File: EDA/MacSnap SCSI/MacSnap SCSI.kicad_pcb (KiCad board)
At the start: 2 copper layers, 84 x 88 mm, 26 parts, among them IC1 Z53C8003VSG, J1 SCSI IDC-50, J2 SCSI IDC-26, U1 MB_LOW, U2 MB_HI, U3 ROM_LOW, U4 ROM_HI, U5 ATF16V8B, U6 ATF16V8B

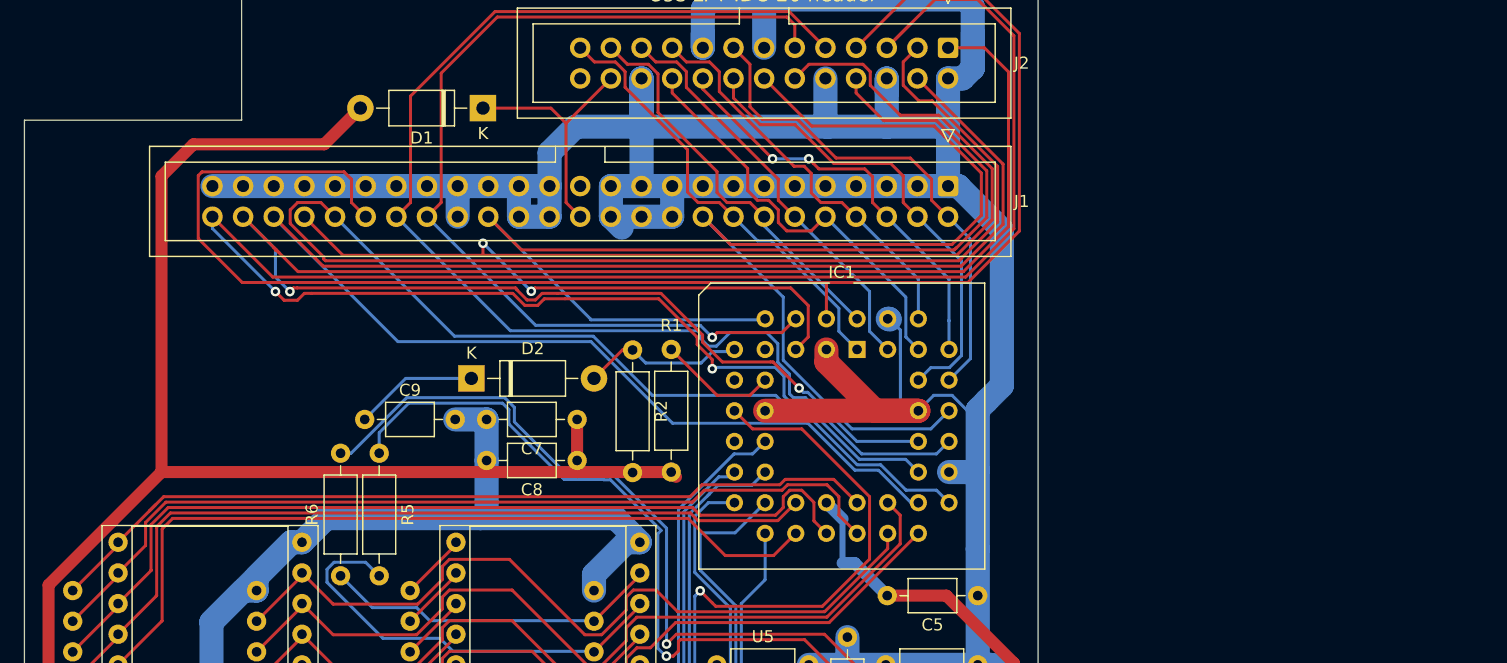
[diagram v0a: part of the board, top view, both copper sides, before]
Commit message: added resistor networks + TMPWR
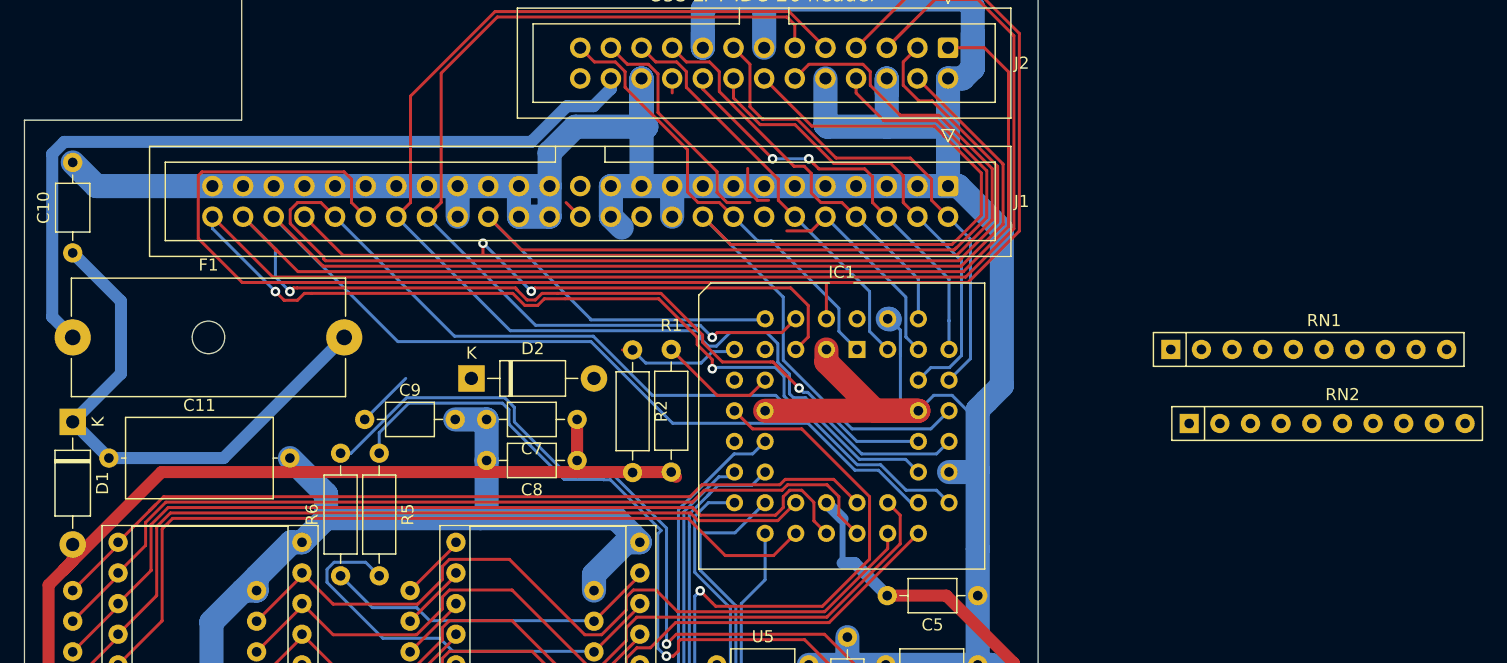
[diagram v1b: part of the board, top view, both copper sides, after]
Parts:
- added C10: 100nF, Capacitor_THT:C_Axial_L3.8mm_D2.6mm_P7.50mm_Horizontal, F.Cu at (64.0, 75.0)
- added C11: 2.2uF, Capacitor_THT:C_Axial_L12.0mm_D6.5mm_P15.00mm_Horizontal, F.Cu at (67.0, 92.0)
- added F1: Fuse 1.25A, Fuse:Fuseholder_Cylinder-5x20mm_Schurter_0031_8201_Horizontal_Open, F.Cu at (64.0, 82.0)
- added RN1: 4610X-101-111LF, Resistor_THT:R_Array_SIP10, F.Cu at (155.0, 83.0)
- added RN2: 4610X-101-111LF, Resistor_THT:R_Array_SIP10, F.Cu at (156.5, 89.1)
- D1: value 1N4001 -> D
- moved D1 42.8 mm to (64.0, 89.0), turned to 270 degrees
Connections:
- D1 pad 1: /TMPWR -> Net-(C10-Pad1)
- J1 pad 26: /TMPWR -> TMPWR
- J2 pad 24: /TMPWR -> TMPWR
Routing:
- net TMPWR: track 0.00 -> 67.0 mm
- net Net-(C10-Pad1): track 0.00 -> 45.2 mm
- net VCC: track 286.1 -> 245.1 mm
- net /TMPWR: track 20.9 -> 0.00 mm
- net /DB6: track 33.0 -> 19.7 mm
- net /DB4: track 35.0 -> 23.0 mm
- net Net-(C9-Pad1): track 10.2 -> 4.81 mm
- net Net-(D2-Pad2): track 13.5 -> 10.2 mm
- net GND: track 493.1 -> 491.6 mm

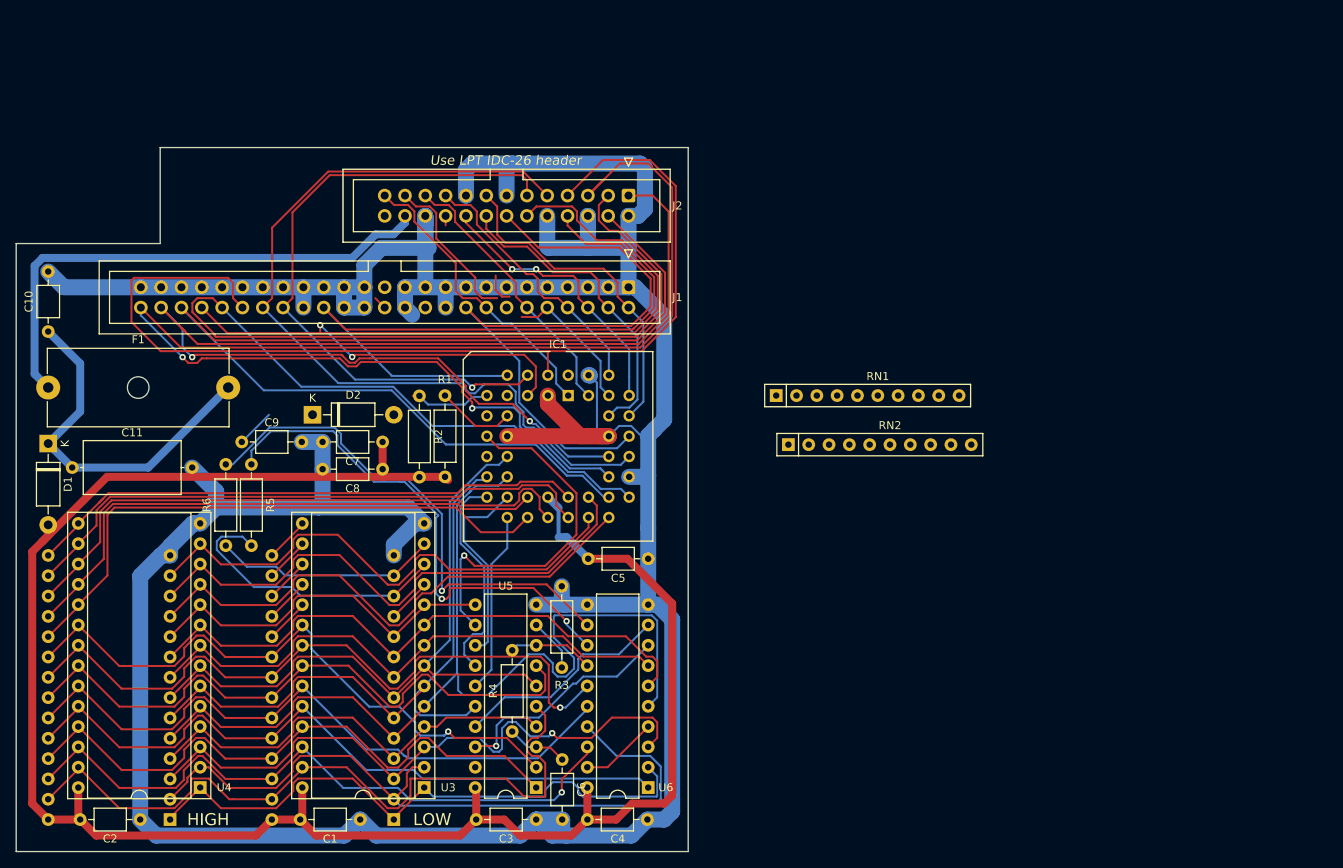
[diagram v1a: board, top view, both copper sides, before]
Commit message: added active SCSI termination to schema
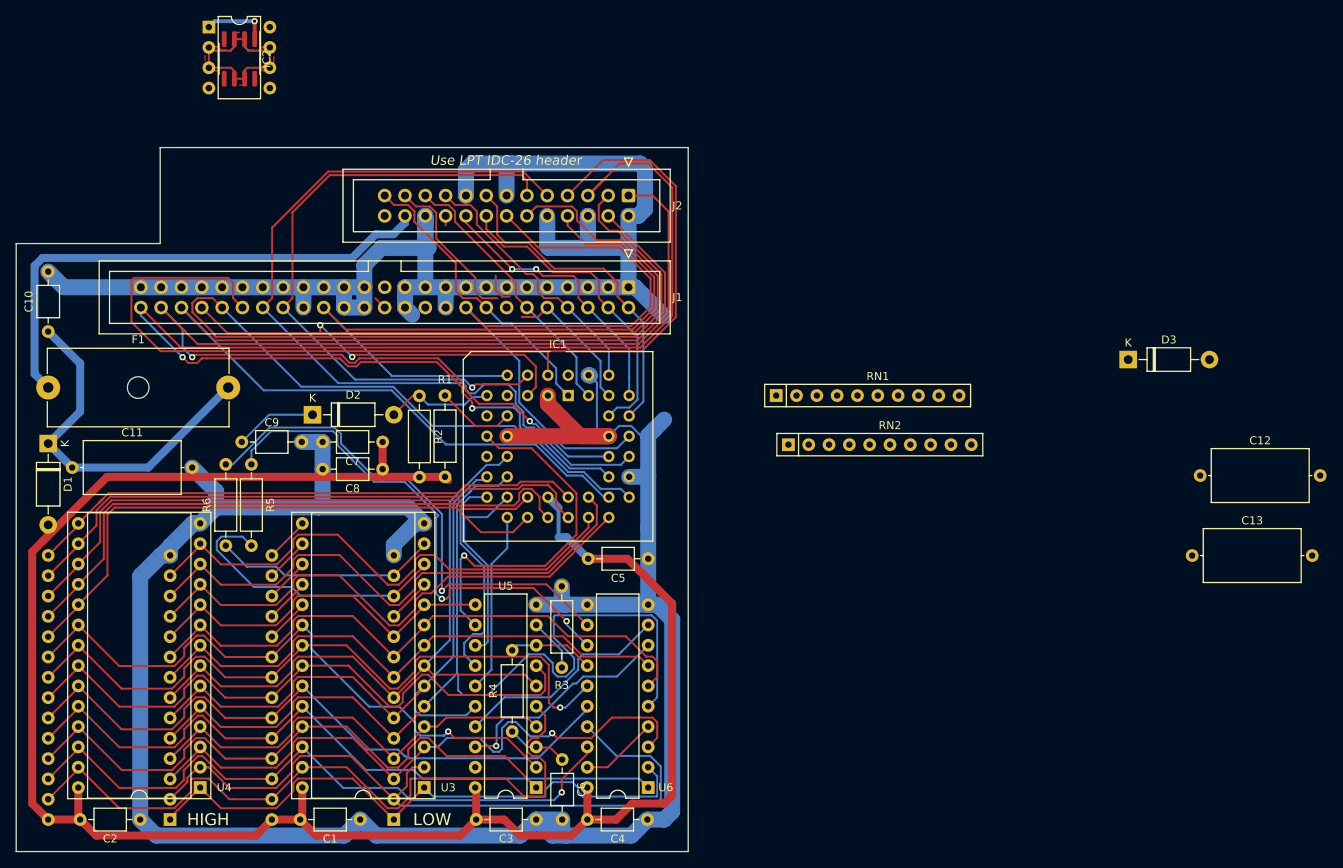
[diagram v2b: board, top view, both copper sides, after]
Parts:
- added C12: 10uF, Capacitor_THT:C_Axial_L12.0mm_D6.5mm_P15.00mm_Horizontal, F.Cu at (208.0, 93.0)
- added C13: 10uF, Capacitor_THT:C_Axial_L12.0mm_D6.5mm_P15.00mm_Horizontal, F.Cu at (207.0, 103.0)
- added D3: 1N5819, Diode_THT:D_DO-41_SOD81_P10.16mm_Horizontal, F.Cu at (199.0, 78.5)
- added IC2: MC34268DR2G, Package_SO:SOIC-8_3.9x4.9mm_P1.27mm, F.Cu at (87.9, 40.9)
- added IC3: MC34268DR2G, Package_DIP:DIP-8_W7.62mm, F.Cu at (84.1, 36.9)
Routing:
- net +2V8: track 0.00 -> 25.3 mm
- net Net-(C9-Pad1): track 4.81 -> 10.2 mm
- net GND: track 491.6 -> 487.0 mm, vias 0 -> 1
- net Net-(D2-Pad2): track 10.2 -> 13.5 mm
- added copper zone on F.Cu, net +2V8

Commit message: removed a few vias and router resistor packs. Moves Z53C80 further down
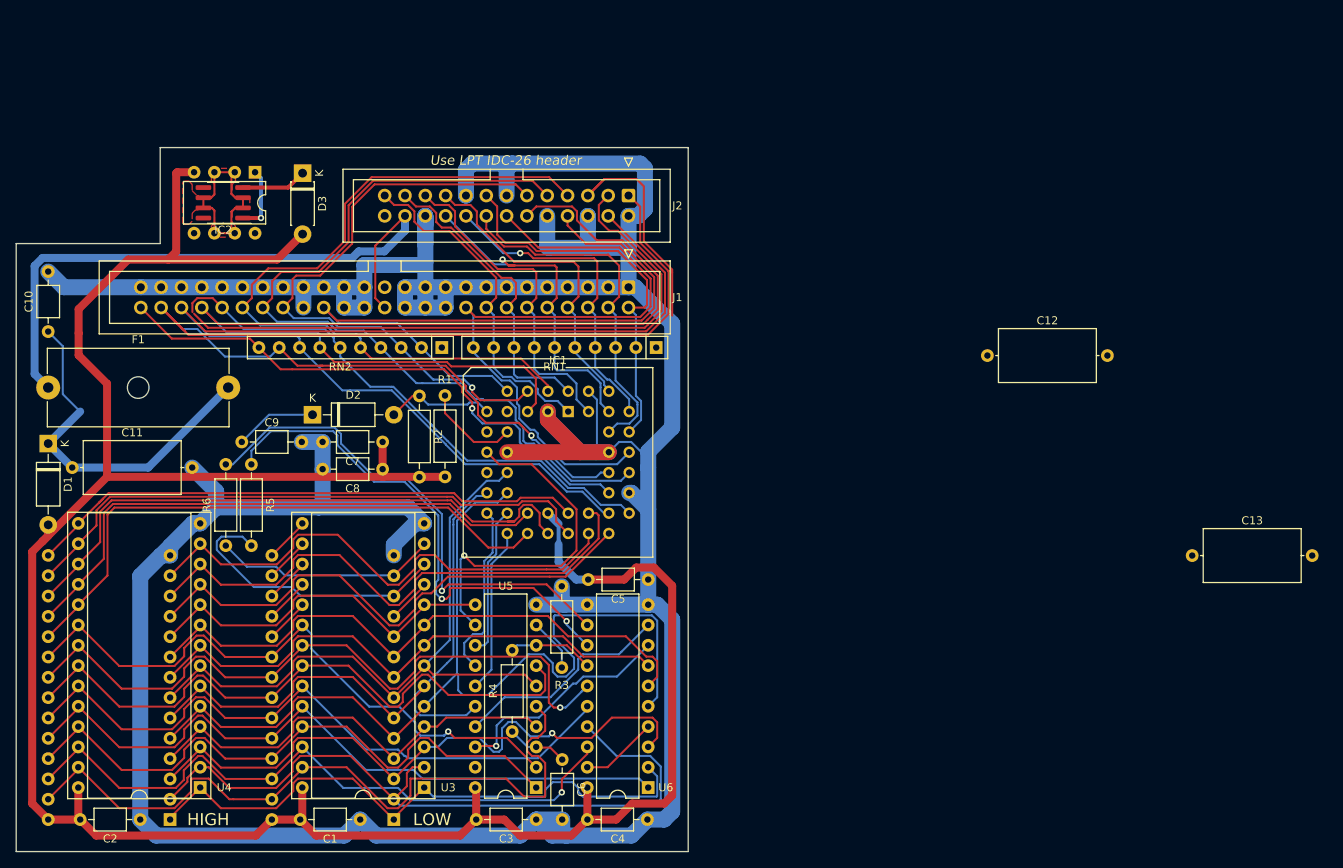
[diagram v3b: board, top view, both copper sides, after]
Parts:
- D3: footprint Diode_THT:D_DO-41_SOD81_P10.16mm_Horizontal -> Diode_THT:D_DO-41_SOD81_P7.62mm_Horizontal
- moved D3 105.8 mm to (95.8, 55.2), turned to 270 degrees
- moved RN2 45.0 mm to (113.2, 77.0), turned to 180 degrees
- moved C12 30.5 mm to (181.4, 78.0)
- moved IC3 19.0 mm to (89.9, 55.1), turned to 270 degrees
- moved IC2 18.1 mm to (85.9, 58.9), turned to 180 degrees
- moved RN1 16.2 mm to (140.0, 77.0), turned to 180 degrees
- moved C5 2.60 mm to (139.0, 106.0)
- moved IC1 2.00 mm to (129.0, 85.0)
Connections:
- RN2 pad 10: /~MSG -> /~IO
- RN2 pad 3: /~SEL -> /~BSY
- RN2 pad 4: /~BSY -> /~ACK
- RN2 pad 6: /~REQ -> /~MSG
- RN2 pad 7: /~ACK -> /~SEL
- RN2 pad 8: /~IO -> /~CD
- RN2 pad 9: /~CD -> /~REQ
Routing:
- net /~IO: track 173.0 -> 99.0 mm, vias 2 -> 1
- net VCC: track 245.1 -> 315.9 mm
- net /~RST: track 129.3 -> 95.6 mm
- net GND: track 487.0 -> 509.7 mm
- net /DB6: track 19.7 -> 39.2 mm
- net /DB4: track 23.0 -> 42.2 mm, vias 0 -> 1
- net /~SEL: track 119.5 -> 135.2 mm, vias 2 -> 0
- net TMPWR: track 67.0 -> 79.4 mm
- net Net-(C12-Pad1): track 0.00 -> 8.20 mm
- net /DB5: track 34.5 -> 42.3 mm
- net /DB0: track 41.7 -> 48.9 mm
- net /~IOR: track 25.0 -> 18.8 mm
- net /DB3: track 33.5 -> 39.6 mm
- net /DB7: track 37.2 -> 43.0 mm
- net /DB1: track 39.7 -> 45.4 mm
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
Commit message: MacSnap SCSI pre-2.0 cleaning
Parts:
- removed C3, C5: 100nF, Capacitor_THT:C_Axial_L3.8mm_D2.6mm_P7.50mm_Horizontal
- removed D1: D, Diode_THT:D_DO-41_SOD81_P10.16mm_Horizontal
- removed D3: 1N5819, Diode_THT:D_DO-41_SOD81_P7.62mm_Horizontal
- removed F1: Fuse 1.25A, Fuse:Fuseholder_Cylinder-5x20mm_Schurter_0031_8201_Horizontal_Open
- removed IC1: Z53C8003VSG, Package_LCC:PLCC-44_THT-Socket
- removed IC2: MC34268DR2G, Package_SO:SOIC-8_3.9x4.9mm_P1.27mm
- removed IC3: MC34268DR2G, Package_DIP:DIP-8_W7.62mm
- removed J2: SCSI IDC-26, Connector_IDC:IDC-Header_2x13_P2.54mm_Vertical
- removed R2: 10k, Resistor_THT:R_Axial_DIN0207_L6.3mm_D2.5mm_P10.16mm_Horizontal
- added C14: 100nF, Capacitor_THT:C_Axial_L3.8mm_D2.6mm_P10.00mm_Horizontal, F.Cu at (111.8, 90.6)
- added G***: LOGO, Misc:Macintosh logo, F.Cu at (67.3, 82.5)
- added G***: LOGO, Misc:SCSI_logo, F.Cu at (81.9, 81.3)
- added R7: 1200, Resistor_THT:R_Axial_DIN0207_L6.3mm_D2.5mm_P10.16mm_Horizontal, F.Cu at (97.2, 83.8)
- added U10: DS1233D, Package_TO_SOT_THT:TO-92_HandSolder, F.Cu at (103.5, 76.8)
- added U7: Z53C8003VSG, Package_LCC:PLCC-44_THT-Socket, F.Cu at (128.9, 82.5)
- added U8: MC34268DR2G, Package_SO:SOIC-8_3.9x4.9mm_P1.27mm, F.Cu at (83.9, 67.9)
- added U9: LT1117-2.85, Package_TO_SOT_SMD:SOT-223-3_TabPin2, F.Cu at (83.8, 57.8)
- C10: value 100nF -> 10uF; footprint Capacitor_THT:C_Axial_L3.8mm_D2.6mm_P7.50mm_Horizontal -> Capacitor_THT:CP_Radial_Tantal_D4.5mm_P2.50mm
- C11: value 2.2uF -> 10uF; footprint Capacitor_THT:C_Axial_L12.0mm_D6.5mm_P15.00mm_Horizontal -> Capacitor_THT:CP_Radial_Tantal_D4.5mm_P2.50mm
- C12: footprint Capacitor_THT:C_Axial_L12.0mm_D6.5mm_P15.00mm_Horizontal -> Capacitor_THT:CP_Radial_Tantal_D4.5mm_P2.50mm
- C13: value 10uF -> 100nF; footprint Capacitor_THT:C_Axial_L12.0mm_D6.5mm_P15.00mm_Horizontal -> Capacitor_THT:C_Axial_L3.8mm_D2.6mm_P10.00mm_Horizontal
- C4: value 100nF -> 1500pF
- C7: value C -> 100nF
- C8, C9: value C -> 10uF; footprint Capacitor_THT:C_Axial_L3.8mm_D2.6mm_P7.50mm_Horizontal -> Capacitor_THT:CP_Radial_Tantal_D4.5mm_P2.50mm
- D2: value 1N4001 -> 1N5817
- J1: value SCSI IDC-50 -> SCSI IDC-26; footprint Connector_IDC:IDC-Header_2x25_P2.54mm_Vertical -> Connector_IDC:IDC-Header_2x13_P2.54mm_Vertical
- moved C13 131.3 mm to (78.9, 74.3)
- moved C12 91.6 mm to (90.8, 64.1)
- moved C8 58.3 mm to (68.0, 136.5), turned to 0 degrees
- moved C7 53.6 mm to (131.5, 135.9), turned to 0 degrees
- moved R6 52.4 mm to (138.4, 106.0), turned to 180 degrees
- moved C2 51.7 mm to (99.8, 95.2)
- moved C1 51.3 mm to (71.8, 95.2), turned to 0 degrees
- moved C9 48.3 mm to (95.9, 136.5)
- moved R5 40.5 mm to (128.3, 102.9), turned to 0 degrees
- moved J1 34.3 mm to (102.2, 69.2), turned to 90 degrees
- moved R3 34.0 mm to (107.3, 90.2), turned to 180 degrees
- moved C11 31.7 mm to (90.8, 71.1)
- moved RN1 29.6 mm to (117.5, 57.8), turned to 0 degrees
- moved RN2 29.5 mm to (90.8, 57.8), turned to 0 degrees
- moved D2 25.3 mm to (74.3, 74.3), turned to 180 degrees
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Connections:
- net /A17 renamed /~{ROM}
- net /~ROMCE renamed /A20
- C1 pad 1: GND -> VCC
- C1 pad 2: VCC -> GND
- C10 pad 1: Net-(C10-Pad1) -> TMPWR
- C11 pad 1: Net-(C10-Pad1) -> +2V8
- C12 pad 1: Net-(C12-Pad1) -> +2V8
- C4 pad 1: VCC -> Net-(U5-I3)
- C6 pad 1: Net-(C6-Pad1) -> VCC
- C9 pad 1: Net-(C9-Pad1) -> VCC
- D2 pad 1: Net-(C9-Pad1) -> TMPWR
- D2 pad 2: Net-(D2-Pad2) -> VCC
- J1 pad 1: GND -> /~{REQ}
- J1 pad 10: /DB4 -> GND
- J1 pad 11: GND -> /~{BSY}
- J1 pad 12: /DB5 -> /~{SEL}
- J1 pad 14: /DB6 -> /PARITY
- J1 pad 15: GND -> /DB0
- J1 pad 16: /DB7 -> /DB1
- J1 pad 18: /PARITY -> /DB2
- J1 pad 19: GND -> /DB3
- J1 pad 2: /DB0 -> GND
- J1 pad 20: GND -> /DB4
- J1 pad 21: GND -> /DB5
- J1 pad 23: GND -> /DB6
- J1 pad 24: GND -> TMPWR
- J1 pad 25: (no net) -> /DB7
- J1 pad 26: TMPWR -> unconnected-(J1-Pin_26-Pad26)
- J1 pad 3: GND -> /~{MSG}
- J1 pad 4: /DB1 -> /~{CD}
- J1 pad 5: GND -> /~{IO}
- J1 pad 6: /DB2 -> GND
- J1 pad 7: GND -> /~{RST}
- J1 pad 8: /DB3 -> /~{ATN}
- J1 pad 9: GND -> /~{ACK}
- R4 pad 1: Net-(C6-Pad1) -> Net-(U5-I3)
- R5 pad 1: Net-(R5-Pad1) -> /D2
- R5 pad 2: /D1 -> Net-(U6-IO8)
- R6 pad 1: /D2 -> Net-(U6-IO7)
- R6 pad 2: Net-(R6-Pad2) -> /D1
- RN1 pad 10: /PARITY -> /DB7
- RN1 pad 2: /DB0 -> /PARITY
- RN1 pad 3: /DB1 -> /DB0
- RN1 pad 4: /DB2 -> /DB1
- RN1 pad 5: /DB3 -> /DB2
- RN1 pad 6: /DB4 -> /DB3
- RN1 pad 7: /DB5 -> /DB4
- RN1 pad 8: /DB6 -> /DB5
- RN1 pad 9: /DB7 -> /DB6
- RN2 pad 10: /~IO -> /~{SEL}
- RN2 pad 2: /~ATN -> /~{REQ}
- RN2 pad 3: /~BSY -> /~{MSG}
- RN2 pad 4: /~ACK -> /~{CD}
- RN2 pad 5: /~RST -> /~{IO}
- RN2 pad 6: /~MSG -> /~{RST}
- RN2 pad 7: /~SEL -> /~{ATN}
- RN2 pad 8: /~CD -> /~{ACK}
- RN2 pad 9: /~REQ -> /~{BSY}
- U5 pad 12: /~DACK -> /~{DACK}
- U5 pad 13: /~IOR -> /~{IOR}
- U5 pad 14: /~CS -> /~{CS}
- U5 pad 15: /~IOW -> /~{IOW}
- U5 pad 17: Net-(U5-Pad17) -> unconnected-(U5-I03-Pad17)
- U5 pad 19: (no net) -> Net-(U5-IO1)
- U5 pad 3: Net-(C6-Pad1) -> Net-(U5-I3)
- U6 pad 12: Net-(R6-Pad2) -> Net-(U6-IO8)
- U6 pad 13: Net-(R5-Pad1) -> Net-(U6-IO7)
- U6 pad 9: Net-(U5-Pad17) -> Net-(U5-IO1)
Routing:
- net /~REQ: track 155.3 -> 0.00 mm, vias 1 -> 0
- net /~MSG: track 147.2 -> 0.00 mm
- net /~CD: track 142.5 -> 0.00 mm
- net /~SEL: track 135.2 -> 0.00 mm
- net /~ACK: track 104.4 -> 0.00 mm
- net /~IO: track 99.0 -> 0.00 mm, vias 1 -> 0
- net /~RST: track 95.6 -> 0.00 mm
- net /~ATN: track 88.5 -> 0.00 mm
- net /~BSY: track 77.6 -> 0.00 mm, vias 1 -> 0
- net +2V8: track 25.3 -> 94.5 mm
- net Net-(R5-Pad1): track 64.4 -> 0.00 mm, vias 2 -> 0
- net Net-(R6-Pad2): track 64.3 -> 0.00 mm, vias 1 -> 0
- net VCC: track 315.9 -> 252.3 mm
- net /~{REQ}: track 0.00 -> 59.3 mm, vias 0 -> 1
- net /~{MSG}: track 0.00 -> 58.1 mm
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- added copper zone on B.Cu, net GND
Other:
- net class Default removed
- net class GND removed
- net class VCC removed
- board text added: "DOV1b"
- board text added: "DOV2"
- board text added: "JLCJLCJLC"
- board text added: "MacSnap SCSI"
- board text added: "MacSnap SCSI Reloaded © 2023 Michel Depeige Based on DOVE MacSnap SCSI https://github.com/demik/oldworld"
- board text added: "Reloaded"
